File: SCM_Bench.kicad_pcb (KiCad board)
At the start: 4 copper layers, 294 parts, among them J1 Conn_Coaxial, J10 RF_Shield_One_Piece, J101 Conn_02x20_Odd_Even, J102 Conn_02x07_Odd_Even, J103 Conn_02x07_Odd_Even, J11 RF_Shield_One_Piece, J12 RF_Shield_One_Piece, J13 Conn_Coaxial, J14 Conn_Coaxial, J15 Conn_Coaxial, J16 Conn_Coaxial, J2 Conn_Coaxial, J3 Conn_Coaxial, J4 Conn_Coaxial, J5 Conn_Coaxial, J6 Conn_Coaxial, J7 RF_Shield_One_Piece, J8 RF_Shield_One_Piece, J9 RF_Shield_One_Piece, SW101 SW_Push, U1 LT6600IS8, U10 LT6600IS8, U101 ASDMB-xxxMHz, U11 LTC2386-18, U12 SN65LVDS1050PW, U13 LT6600IS8, U14 LTC2386-18, U15 SN65LVDS1050PW, U16 AD9747BCPZ, U17 SN65LVDS1DBV, U18 AD8021, U19 AD8021, U2 LTC2386-18, U20 AD9747BCPZ, U21 SN65LVDS1DBV, U22 AD8021, U23 AD8021, U3 SN65LVDS1050PW, U301 LT6600IS8, U302 LTC2386-18, U303 SN65LVDS1050PW, U4 LT6600IS8, U5 LTC2386-18, U6 SN65LVDS1050PW, U7 LT6600IS8, U8 LTC2386-18, U9 SN65LVDS1050PW

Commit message: initial placement of all ADC/DAC blocks and added FPGA
Signed-off-by: Alexis Jeandet <alexis.jeandet@member.fsf.org>
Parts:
- added C114: 100nF, Capacitor_SMD:C_0402_1005Metric, F.Cu at (56.0, 152.0)
- added C115: 100nF, Capacitor_SMD:C_0402_1005Metric, F.Cu at (53.1, 148.0)
- added C116: 100nF, Capacitor_SMD:C_0402_1005Metric, F.Cu at (53.1, 150.0)
- added C117: 100nF, Capacitor_SMD:C_0402_1005Metric, F.Cu at (56.0, 148.0)
- added C118: 100nF, Capacitor_SMD:C_0402_1005Metric, F.Cu at (60.4, 145.5)
- added C119: 100nF, Capacitor_SMD:C_0402_1005Metric, F.Cu at (53.1, 152.0)
- added C120: 100nF, Capacitor_SMD:C_0402_1005Metric, F.Cu at (56.0, 150.0)
- added C121: 100nF, Capacitor_SMD:C_0402_1005Metric, F.Cu at (58.9, 147.5)
- added C122: 100nF, Capacitor_SMD:C_0402_1005Metric, F.Cu at (53.1, 154.0)
- added C123: 100nF, Capacitor_SMD:C_0402_1005Metric, F.Cu at (63.3, 145.5)
- added C124: 100nF, Capacitor_SMD:C_0402_1005Metric, F.Cu at (58.9, 149.5)
- added C125: 100nF, Capacitor_SMD:C_0402_1005Metric, F.Cu at (57.4, 145.5)
- added C126: 100nF, Capacitor_SMD:C_0402_1005Metric, F.Cu at (61.8, 147.5)
- added C127: 100nF, Capacitor_SMD:C_0402_1005Metric, F.Cu at (53.1, 156.0)
- added C128: 100nF, Capacitor_SMD:C_0402_1005Metric, F.Cu at (56.0, 154.0)
- added C129: 100nF, Capacitor_SMD:C_0402_1005Metric, F.Cu at (58.9, 151.5)
- added C130: 100nF, Capacitor_SMD:C_0402_1005Metric, F.Cu at (66.2, 145.5)
- added C131: 100nF, Capacitor_SMD:C_0402_1005Metric, F.Cu at (53.1, 158.0)
- added DONE1: LED, Resistor_SMD:R_0603_1608Metric_Pad1.05x0.95mm_HandSolder, F.Cu at (53.8, 145.8)
- added R100: 10k, Resistor_SMD:R_0402_1005Metric, F.Cu at (61.8, 149.5)
- added R104: 10k, Resistor_SMD:R_0402_1005Metric, F.Cu at (64.7, 147.5)
- added R105: 2K2, Resistor_SMD:R_0402_1005Metric, F.Cu at (56.0, 156.0)
- added U24: ICE40HX1K-4K-TQ144, Package_QFP:TQFP-144_20x20mm_P0.5mm, F.Cu at (86.0, 152.0)
- C1, C10, C12, C13, C14, C15, C18, C19, C2, C20, C23, C25, C26, C301, C302, C305, C306, C307, C310, C312, C313, C5, C6, C7, J1, J2, J3, J7, J8, J9, R1, R11, R12, R14, R15, R16, R17, R18, R19, R2, R21, R24, R25, R3, R301, R302, R303, R304, R305, R306, R309, R311, R312, R4, R5, R6, R8, U1, U3, U301, U303, U4, U6: moved to B.Cu
- C11, C16, C17, C21, C22, C24, C3, C303, C304, C308, C309, C311, C4, C8, C9, R10, R13, R20, R22, R23, R26, R307, R308, R310, R313, R7, R9, U2, U302, U5: moved to F.Cu
- moved J16 345.7 mm to (141.2, 159.6), turned to 270 degrees
- moved J15 344.1 mm to (141.1, 169.1), turned to 270 degrees
- moved C107 332.1 mm to (131.2, 158.5), turned to 0 degrees
- moved R93 331.6 mm to (131.3, 161.1), turned to 180 degrees
- moved U22 331.5 mm to (131.3, 161.7), turned to 0 degrees
- moved C108 330.8 mm to (131.0, 163.6), turned to 0 degrees
- moved U23 330.6 mm to (131.3, 166.9), turned to 0 degrees
- moved C112 330.5 mm to (131.0, 165.0), turned to 0 degrees
- moved R99 330.5 mm to (131.3, 167.5), turned to 180 degrees
- moved C111 330.0 mm to (131.2, 170.2), turned to 0 degrees
- moved C109 327.6 mm to (128.1, 158.5), turned to 180 degrees
- moved C113 325.5 mm to (128.1, 170.2), turned to 180 degrees
- moved R90 324.2 mm to (126.0, 161.0), turned to 180 degrees
- moved R91 323.9 mm to (126.0, 162.5), turned to 180 degrees
- moved R92 323.9 mm to (126.0, 162.5), turned to 0 degrees
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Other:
- board outline added: 86 x 145 mm

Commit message: Layout done for ADC + LVDS and DAC -> FPGA
Signed-off-by: Alexis Jeandet <alexis.jeandet@member.fsf.org>
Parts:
- added C132: 100nF, Capacitor_SMD:C_0402_1005Metric, F.Cu at (103.9, 164.4)
- added J17: Conn_01x06, Connector_PinHeader_2.54mm:PinHeader_1x06_P2.54mm_Vertical, F.Cu at (80.2, 183.7)
- added R106: 10k, Resistor_SMD:R_0402_1005Metric, F.Cu at (105.3, 166.8)
- added R107: 10k, Resistor_SMD:R_0402_1005Metric, B.Cu at (96.3, 168.5)
- added R108: 10k, Resistor_SMD:R_0402_1005Metric, B.Cu at (96.6, 166.0)
- added U25: M25PX32-VMW, Package_SO:SOIJ-8_5.3x5.3mm_P1.27mm, F.Cu at (99.8, 167.9)
- C114, C116, C117, C118, C119, C120, C121, C124, C125, C126, C127, C129, C130, C131, R100, R104, R105, R38: moved to B.Cu
- R312: moved to F.Cu
- moved C101 69.6 mm to (55.6, 71.2)
- moved C102 69.6 mm to (43.7, 78.2)
- moved D101 69.6 mm to (53.4, 69.0)
- moved D102 69.6 mm to (44.4, 75.9)
- moved H101 69.6 mm to (47.7, 71.2)
- moved H102 69.6 mm to (38.8, 76.3)
- moved R101 69.6 mm to (46.6, 79.6)
- moved R102 69.6 mm to (57.0, 68.7)
- moved R103 69.6 mm to (52.7, 71.2)
- moved SW101 69.6 mm to (39.8, 70.3)
- moved U101 69.6 mm to (48.6, 76.7)
- moved R39 51.0 mm to (64.1, 67.2), turned to 90 degrees
- moved C38 48.5 mm to (66.9, 70.0), turned to 180 degrees
- moved U9 46.3 mm to (69.0, 66.3), turned to 180 degrees
- moved C115 45.5 mm to (96.2, 162.8)
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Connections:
- J1 pad 1: /Sheet5F3E1819/CH1_IN+ -> /Sheet5F3E1819/CH2_IN+
- J1 pad 2: /Sheet5F3E1819/CH1_IN- -> /Sheet5F3E1819/CH2_IN-
- J2 pad 1: /Sheet5F3E1819/CH2_IN+ -> /Sheet5F3E1819/CH6_IN+
- J2 pad 2: /Sheet5F3E1819/CH2_IN- -> /Sheet5F3E1819/CH6_IN-
- J3 pad 1: /Sheet5F3E1819/CH3_IN+ -> /Sheet5F3E1819/CH4_IN+
- J3 pad 2: /Sheet5F3E1819/CH3_IN- -> /Sheet5F3E1819/CH4_IN-
- J4 pad 1: /Sheet5F3E1819/CH4_IN+ -> /Sheet5F3E1819/CH1_IN+
- J4 pad 2: /Sheet5F3E1819/CH4_IN- -> /Sheet5F3E1819/CH1_IN-
- J6 pad 1: /Sheet5F3E1819/CH6_IN+ -> /Sheet5F3E1819/CH3_IN+
- J6 pad 2: /Sheet5F3E1819/CH6_IN- -> /Sheet5F3E1819/CH3_IN-
- R1 pad 2: /Sheet5F3E1819/CH2_IN+ -> /Sheet5F3E1819/CH6_IN+
- R104 pad 1: /Sheet5F420A25/sheet5F62EEDA/FLASH_SS -> VCCIO_0
- R104 pad 2: GND -> /Sheet5F420A25/sheet5F62EEDA/FLASH_CLK
- R14 pad 2: /Sheet5F3E1819/CH3_IN+ -> /Sheet5F3E1819/CH4_IN+
- R15 pad 2: /Sheet5F3E1819/CH3_IN- -> /Sheet5F3E1819/CH4_IN-
- R2 pad 2: /Sheet5F3E1819/CH2_IN- -> /Sheet5F3E1819/CH6_IN-
- R27 pad 2: /Sheet5F3E1819/CH4_IN+ -> /Sheet5F3E1819/CH1_IN+
- R28 pad 2: /Sheet5F3E1819/CH4_IN- -> /Sheet5F3E1819/CH1_IN-
- R301 pad 2: /Sheet5F3E1819/CH1_IN+ -> /Sheet5F3E1819/CH2_IN+
- R302 pad 2: /Sheet5F3E1819/CH1_IN- -> /Sheet5F3E1819/CH2_IN-
- R53 pad 2: /Sheet5F3E1819/CH6_IN+ -> /Sheet5F3E1819/CH3_IN+
- R54 pad 2: /Sheet5F3E1819/CH6_IN- -> /Sheet5F3E1819/CH3_IN-
- U16 pad 10: (no net) -> /Sheet5F420A25/DAC1_D14
- U16 pad 11: (no net) -> /Sheet5F420A25/DAC1_D13
- U16 pad 12: (no net) -> /Sheet5F420A25/DAC1_D12
- U16 pad 13: (no net) -> /Sheet5F420A25/DAC1_D11
- U16 pad 14: (no net) -> /Sheet5F420A25/DAC1_D10
- U16 pad 15: (no net) -> /Sheet5F420A25/DAC1_D9
- U16 pad 16: (no net) -> /Sheet5F420A25/DAC1_D8
- U16 pad 17: (no net) -> /Sheet5F420A25/DAC1_D7
- U16 pad 18: (no net) -> /Sheet5F420A25/DAC1_D6
- U16 pad 19: (no net) -> /Sheet5F420A25/DAC1_D5
- U16 pad 20: (no net) -> /Sheet5F420A25/DAC1_D4
- U16 pad 21: (no net) -> /Sheet5F420A25/DAC1_D3
- U16 pad 22: (no net) -> /Sheet5F420A25/DAC1_D2
- U16 pad 23: (no net) -> /Sheet5F420A25/DAC1_D1
- U16 pad 24: (no net) -> /Sheet5F420A25/DAC1_D0
- U16 pad 25: (no net) -> /Sheet5F420A25/sheet5F62EEDA/DAC1_DCO
- U16 pad 29: (no net) -> /Sheet5F420A25/sheet5F62EEDA/DAC1_IQSEL
- U16 pad 49: (no net) -> /Sheet5F420A25/sheet5F62EEDA/DAC1_SDO
- U16 pad 50: (no net) -> /Sheet5F420A25/sheet5F62EEDA/DAC1_SDIO
- U16 pad 51: (no net) -> /Sheet5F420A25/sheet5F62EEDA/DAC1_SCLK
- U16 pad 52: (no net) -> /Sheet5F420A25/Sheet5F420DB3/CSB
- U16 pad 53: (no net) -> /Sheet5F420A25/sheet5F62EEDA/DAC1_RST
- U16 pad 9: (no net) -> /Sheet5F420A25/DAC1_D15
- U17 pad 5: (no net) -> /Sheet5F420A25/sheet5F62EEDA/DAC1_CLK
- U20 pad 10: (no net) -> /Sheet5F420A25/DAC2_D14
- U20 pad 11: (no net) -> /Sheet5F420A25/DAC2_D13
- U20 pad 12: (no net) -> /Sheet5F420A25/DAC2_D12
- U20 pad 13: (no net) -> /Sheet5F420A25/DAC2_D11
- U20 pad 14: (no net) -> /Sheet5F420A25/DAC2_D10
- U20 pad 15: (no net) -> /Sheet5F420A25/DAC2_D9
- U20 pad 16: (no net) -> /Sheet5F420A25/DAC2_D8
- U20 pad 17: (no net) -> /Sheet5F420A25/DAC2_D7
- U20 pad 18: (no net) -> /Sheet5F420A25/DAC2_D6
- U20 pad 19: (no net) -> /Sheet5F420A25/DAC2_D5
- U20 pad 20: (no net) -> /Sheet5F420A25/DAC2_D4
- U20 pad 21: (no net) -> /Sheet5F420A25/DAC2_D3
- U20 pad 22: (no net) -> /Sheet5F420A25/DAC2_D2
- U20 pad 23: (no net) -> /Sheet5F420A25/DAC2_D1
- U20 pad 24: (no net) -> /Sheet5F420A25/DAC2_D0
- U20 pad 25: (no net) -> /Sheet5F420A25/sheet5F62EEDA/DAC2_DCO
- U20 pad 29: (no net) -> /Sheet5F420A25/sheet5F62EEDA/DAC2_IQSEL
- U20 pad 49: (no net) -> /Sheet5F420A25/sheet5F62EEDA/DAC2_SDO
- U20 pad 50: (no net) -> /Sheet5F420A25/sheet5F62EEDA/DAC2_SDIO
- U20 pad 51: (no net) -> /Sheet5F420A25/sheet5F62EEDA/DAC2_SCLK
- U20 pad 52: (no net) -> /Sheet5F420A25/sheet5F604603/CSB
- U20 pad 53: (no net) -> /Sheet5F420A25/sheet5F62EEDA/DAC2_RST
- U20 pad 9: (no net) -> /Sheet5F420A25/DAC2_D15
- U21 pad 5: (no net) -> /Sheet5F420A25/sheet5F62EEDA/DAC2_CLK
- U24 pad 101: (no net) -> /Sheet5F420A25/sheet5F62EEDA/DAC2_CLK
- U24 pad 102: (no net) -> /Sheet5F420A25/sheet5F62EEDA/DAC1_RST
- U24 pad 104: (no net) -> /Sheet5F420A25/Sheet5F420DB3/CSB
- U24 pad 105: (no net) -> /Sheet5F420A25/sheet5F62EEDA/DAC1_SCLK
- U24 pad 106: (no net) -> /Sheet5F420A25/sheet5F62EEDA/DAC1_SDIO
- U24 pad 107: (no net) -> /Sheet5F420A25/sheet5F62EEDA/DAC1_SDO
- U24 pad 112: (no net) -> /Sheet5F420A25/sheet5F62EEDA/DAC1_IQSEL
- U24 pad 113: (no net) -> /Sheet5F420A25/DAC1_D0
- U24 pad 114: (no net) -> /Sheet5F420A25/DAC1_D1
- U24 pad 115: (no net) -> /Sheet5F420A25/DAC1_D2
- U24 pad 116: (no net) -> /Sheet5F420A25/DAC1_D3
- U24 pad 117: (no net) -> /Sheet5F420A25/DAC1_D4
- U24 pad 118: (no net) -> /Sheet5F420A25/DAC1_D5
- U24 pad 119: (no net) -> /Sheet5F420A25/DAC1_D6
- U24 pad 120: (no net) -> /Sheet5F420A25/DAC1_D7
- U24 pad 121: (no net) -> /Sheet5F420A25/DAC1_D8
- U24 pad 122: (no net) -> /Sheet5F420A25/DAC1_D9
- U24 pad 128: (no net) -> /Sheet5F420A25/sheet5F62EEDA/DAC1_DCO
- U24 pad 129: (no net) -> /Sheet5F420A25/DAC1_D10
- U24 pad 134: (no net) -> /Sheet5F420A25/DAC1_D11
- U24 pad 135: (no net) -> /Sheet5F420A25/DAC1_D12
- U24 pad 136: (no net) -> /Sheet5F420A25/DAC1_D13
- U24 pad 137: (no net) -> /Sheet5F420A25/DAC1_D14
- U24 pad 138: (no net) -> /Sheet5F420A25/DAC1_D15
- U24 pad 139: (no net) -> /Sheet5F420A25/sheet5F62EEDA/DAC1_CLK
- U24 pad 58: (no net) -> /Sheet5F420A25/sheet5F604603/CSB
- U24 pad 60: (no net) -> /Sheet5F420A25/sheet5F62EEDA/DAC2_SCLK
- U24 pad 61: (no net) -> /Sheet5F420A25/sheet5F62EEDA/DAC2_SDIO
- U24 pad 62: (no net) -> /Sheet5F420A25/sheet5F62EEDA/DAC2_SDO
- U24 pad 67: (no net) -> /Sheet5F420A25/sheet5F62EEDA/FLASH_MISO
- U24 pad 68: (no net) -> /Sheet5F420A25/sheet5F62EEDA/FLASH_MOSI
- U24 pad 70: (no net) -> /Sheet5F420A25/sheet5F62EEDA/FLASH_CLK
- U24 pad 73: (no net) -> /Sheet5F420A25/sheet5F62EEDA/DAC2_RST
- U24 pad 74: (no net) -> /Sheet5F420A25/sheet5F62EEDA/DAC2_IQSEL
- U24 pad 75: (no net) -> /Sheet5F420A25/DAC2_D0
- U24 pad 76: (no net) -> /Sheet5F420A25/DAC2_D1
- U24 pad 78: (no net) -> /Sheet5F420A25/DAC2_D2
- U24 pad 79: (no net) -> /Sheet5F420A25/DAC2_D3
- U24 pad 80: (no net) -> /Sheet5F420A25/DAC2_D4
- U24 pad 81: (no net) -> /Sheet5F420A25/DAC2_D5
- U24 pad 87: (no net) -> /Sheet5F420A25/DAC2_D6
- U24 pad 88: (no net) -> /Sheet5F420A25/DAC2_D7
- U24 pad 90: (no net) -> /Sheet5F420A25/DAC2_D8
- U24 pad 91: (no net) -> /Sheet5F420A25/DAC2_D9
- U24 pad 93: (no net) -> /Sheet5F420A25/sheet5F62EEDA/DAC2_DCO
- U24 pad 94: (no net) -> /Sheet5F420A25/DAC2_D10
- U24 pad 95: (no net) -> /Sheet5F420A25/DAC2_D11
- U24 pad 96: (no net) -> /Sheet5F420A25/DAC2_D12
- U24 pad 97: (no net) -> /Sheet5F420A25/DAC2_D13
- U24 pad 98: (no net) -> /Sheet5F420A25/DAC2_D14
- U24 pad 99: (no net) -> /Sheet5F420A25/DAC2_D15
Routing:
- net /Sheet5F3E1819/sheet5F7672A2/CNV+: track 0.00 -> 92.7 mm, vias 0 -> 1
- net /Sheet5F3E1819/sheet5F7672A2/CNV-: track 0.00 -> 89.5 mm, vias 0 -> 1
- net /Sheet5F3E1819/sheet5F7672A2/CLK+: track 2.41 -> 75.3 mm, vias 0 -> 1
- net /Sheet5F3E1819/sheet5F7672A2/CLK-: track 2.78 -> 75.1 mm, vias 0 -> 1
- net /Sheet5F3E1819/sheet5F7672A2/DCO+: track 0.00 -> 65.4 mm, vias 0 -> 1
- net /Sheet5F3E1819/sheet5F7672A2/DA+: track 0.00 -> 65.0 mm, vias 0 -> 1
- net /Sheet5F3E1819/sheet5F7672A2/DA-: track 0.00 -> 64.7 mm, vias 0 -> 1
- net /Sheet5F3E1819/sheet5F7672A2/DCO-: track 0.00 -> 63.0 mm, vias 0 -> 1
- net /Sheet5F3E1819/Sheet5F3E1AE4/DA-: track 0.00 -> 49.7 mm, vias 0 -> 1
- net /Sheet5F3E1819/Sheet5F3E1AE4/DA+: track 0.00 -> 48.1 mm, vias 0 -> 1
- net /Sheet5F420A25/sheet5F62EEDA/DAC1_CLK: track 0.00 -> 47.6 mm, vias 0 -> 2
- net /Sheet5F420A25/DAC1_D15: track 0.00 -> 46.2 mm
- net /Sheet5F420A25/DAC1_D14: track 0.00 -> 44.4 mm
- net /Sheet5F420A25/DAC1_D13: track 0.00 -> 42.7 mm
- net /Sheet5F420A25/DAC1_D12: track 0.00 -> 41.0 mm
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
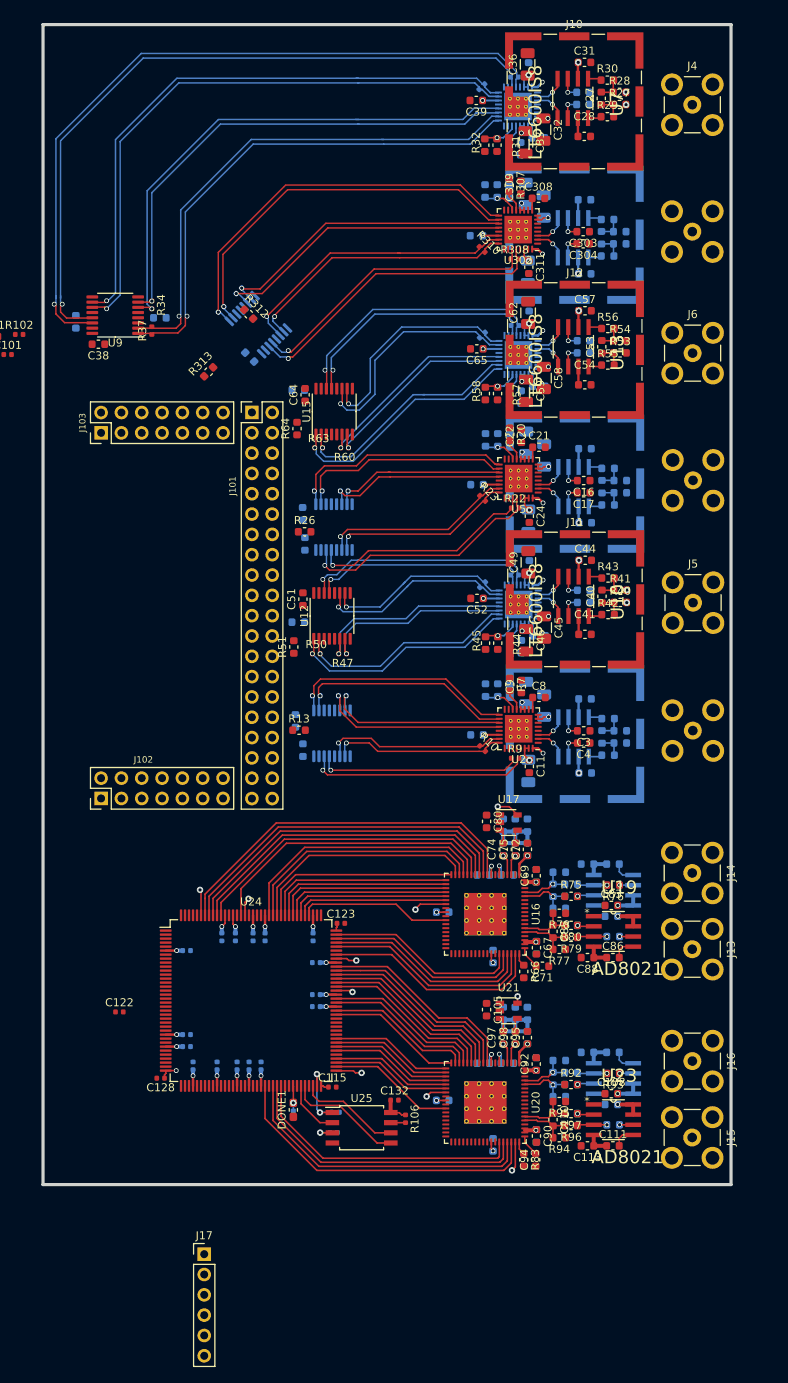
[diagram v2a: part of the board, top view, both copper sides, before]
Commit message: Added #3.3V and #1.2V supply, completed ADC to USB board layout, added DAC FPGA to USB board bus.
Signed-off-by: Alexis Jeandet <alexis.jeandet@member.fsf.org>
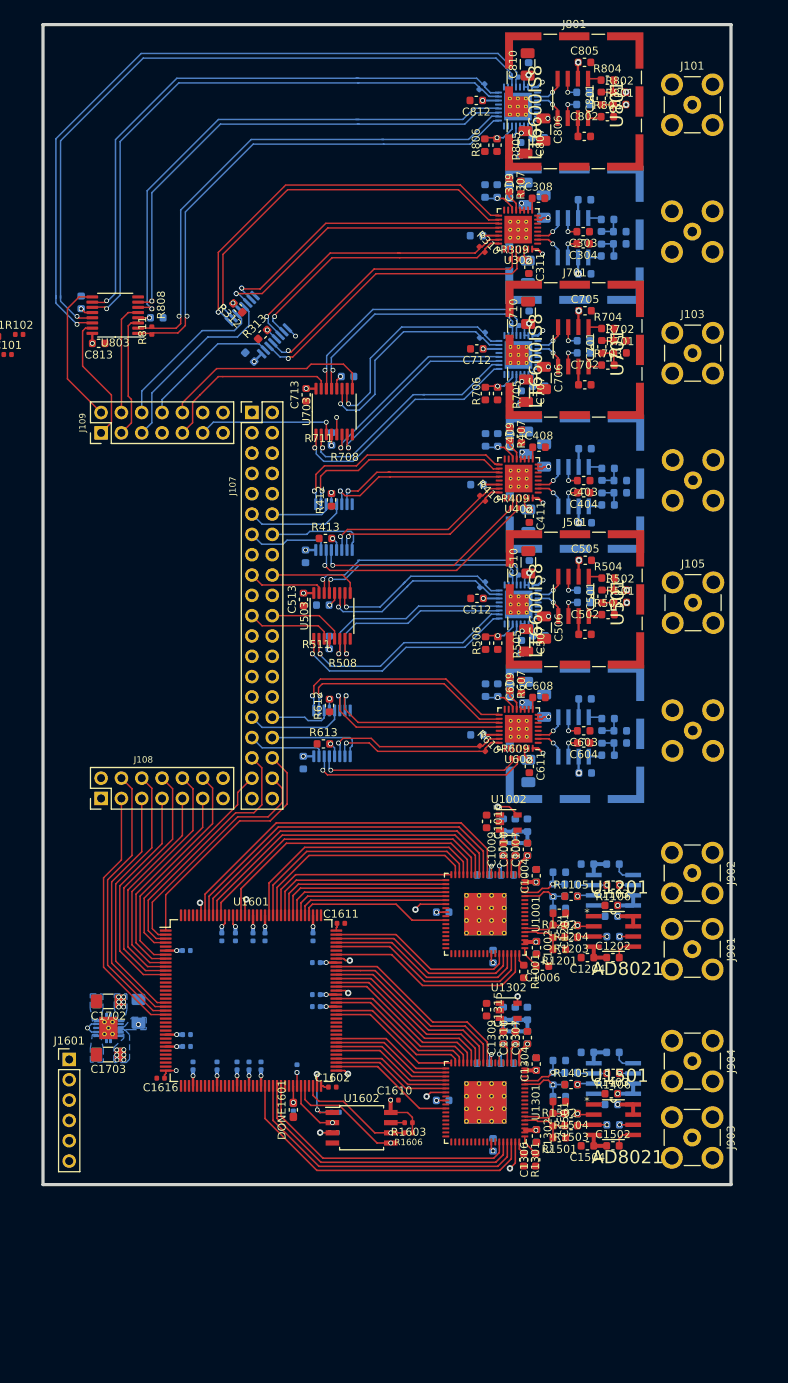
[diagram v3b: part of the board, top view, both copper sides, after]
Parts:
- removed C122: 100nF, Capacitor_SMD:C_0402_1005Metric
- removed R38: 10k, Resistor_SMD:R_0603_1608Metric
- added C1609: 100nF, Capacitor_SMD:C_0402_1005Metric, B.Cu at (77.9, 145.7)
- added C1620: 100nF, Capacitor_SMD:C_0402_1005Metric, B.Cu at (78.0, 157.7)
- added C1701: 10uF, Capacitor_SMD:C_1206_3216Metric_Pad1.42x1.75mm_HandSolder, B.Cu at (71.9, 153.3)
- added C1702: 10uF, Capacitor_SMD:C_1206_3216Metric_Pad1.42x1.75mm_HandSolder, F.Cu at (68.2, 152.1)
- added C1703: 10uF, Capacitor_SMD:C_1206_3216Metric_Pad1.42x1.75mm_HandSolder, F.Cu at (68.2, 158.8)
- added L1701: 2.2uH, Inductor_SMD:L_1206_3216Metric_Pad1.42x1.75mm_HandSolder, B.Cu at (68.2, 158.8)
- added L1702: 2.2uH, Inductor_SMD:L_1206_3216Metric_Pad1.42x1.75mm_HandSolder, B.Cu at (68.2, 152.1)
- added R812: 10k, Resistor_SMD:R_0603_1608Metric, B.Cu at (74.2, 66.6)
- added U1701: tps6240x, Package_SON:Texas_S-PVSON-N10_ThermalVias, B.Cu at (68.2, 155.4)
- R1606: renamed from R104; moved to F.Cu
- R412: renamed from R25; moved to F.Cu
- R512: renamed from R51; moved to B.Cu
- R612: renamed from R12; moved to F.Cu
- R712: renamed from R64; moved to B.Cu
- moved R1606 35.9 mm to (105.7, 168.5), turned to 180 degrees
- moved J1601 29.6 mm to (63.3, 159.4)
- moved R1601 14.1 mm to (91.7, 160.5), turned to 270 degrees
- moved R313 8.21 mm to (87.5, 68.7)
- moved R713 6.40 mm to (98.1, 74.0), turned to 180 degrees
- moved R612 4.67 mm to (95.8, 115.1), turned to 90 degrees
- moved R712 4.50 mm to (96.1, 81.8), turned to 270 degrees
- moved R512 4.47 mm to (95.8, 107.2), turned to 270 degrees
- moved R412 4.01 mm to (96.1, 89.4), turned to 90 degrees
- moved R513 3.74 mm to (95.0, 102.6)
- moved R613 3.50 mm to (95.0, 119.9)
- moved R413 2.73 mm to (95.3, 94.2)
- moved R813 2.52 mm to (64.8, 64.7), turned to 270 degrees
- moved R312 1.56 mm to (84.4, 65.4), turned to 135 degrees
- moved C413 1.56 mm to (92.8, 96.5), turned to 90 degrees
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- renumbered C66 to C1001, C67 to C1002, C68 to C1003, C69 to C1004, C70 to C1005, C71 to C1006, C72 to C1007, C73 to C1008, C74 to C1009, C75 to C1010, C76 to C1011, C77 to C1012, C78 to C1013, C79 to C1014, C80 to C1015, C81 to C1101, C82 to C1102, C83 to C1103, C84 to C1104, C85 to C1201, C86 to C1202, C87 to C1203, C88 to C1204, C89 to C1301, C90 to C1302, C91 to C1303, C92 to C1304, C93 to C1305, C94 to C1306, C95 to C1307, C96 to C1308, C97 to C1309, C98 to C1310, C99 to C1311, C100 to C1312, C103 to C1313, C104 to C1314, C105 to C1315, C106 to C1401, C107 to C1402, C108 to C1403, C109 to C1404, C110 to C1501, C111 to C1502, C112 to C1503, C113 to C1504, C114 to C1601, C115 to C1602, C116 to C1603, C117 to C1604, C118 to C1605, C119 to C1606, C120 to C1607, C121 to C1608, C132 to C1610, C123 to C1611, C124 to C1612, C125 to C1613, C126 to C1614, C127 to C1615, C128 to C1616, C129 to C1617, C130 to C1618, C131 to C1619, C307 to C305, C305 to C306, C306 to C307, C14 to C401, C15 to C402, C16 to C403, C17 to C404, C18 to C405, C19 to C406, C20 to C407, C21 to C408, C22 to C409, C23 to C410, C24 to C411, C26 to C412, C25 to C413, C40 to C501, C41 to C502, C42 to C503, C43 to C504, C44 to C505, C45 to C506, C46 to C507, C47 to C508, C48 to C509, C49 to C510, C50 to C511, C52 to C512, C51 to C513, C1 to C601, C2 to C602, C3 to C603, C4 to C604, C5 to C605, C6 to C606, C7 to C607, C8 to C608, C9 to C609, C10 to C610, C11 to C611, C13 to C612, C12 to C613, C53 to C701, C54 to C702, C55 to C703, C56 to C704, C57 to C705, C58 to C706, C59 to C707, C60 to C708, C61 to C709, C62 to C710, C63 to C711, C65 to C712, C64 to C713, C27 to C801, C28 to C802, C29 to C803, C30 to C804, C31 to C805, C32 to C806, C33 to C807, C34 to C808, C35 to C809, C36 to C810, C37 to C811, C39 to C812, C38 to C813, DONE1 to DONE1601, J4 to J101, J1 to J102, J6 to J103, J3 to J104, J5 to J105, J2 to J106, J101 to J107, J102 to J108, J103 to J109, J17 to J1601, J7 to J301, J9 to J401, J11 to J501, J8 to J601, J12 to J701, J10 to J801, J13 to J901, J14 to J902, J15 to J903, J16 to J904, R66 to R1001, R67 to R1002, R68 to R1003, R69 to R1004, R70 to R1005, R71 to R1101, R72 to R1102, R73 to R1103, R74 to R1104, R75 to R1105, R76 to R1106, R77 to R1201, R78 to R1202, R79 to R1203, R80 to R1204, R81 to R1205, R82 to R1206, R83 to R1301, R84 to R1302, R85 to R1303, R86 to R1304, R87 to R1305, R88 to R1401, R89 to R1402, R90 to R1403, R91 to R1404, R92 to R1405, R93 to R1406, R94 to R1501, R95 to R1502, R96 to R1503, R97 to R1504, R98 to R1505, R99 to R1506, R100 to R1601, R105 to R1602, R106 to R1603, R107 to R1604, R108 to R1605, R309 to R308, R308 to R309, R14 to R401, R15 to R402, R16 to R403, R17 to R404, R18 to R405, R19 to R406, R20 to R407, R21 to R408, R22 to R409, R23 to R410, R24 to R411, R26 to R413, R40 to R501, R41 to R502, R42 to R503, R43 to R504, R44 to R505, R45 to R506, R46 to R507, R47 to R508, R48 to R509, R49 to R510, R50 to R511, R52 to R513, R1 to R601, R2 to R602, R3 to R603, R4 to R604, R5 to R605, R6 to R606, R7 to R607, R8 to R608, R9 to R609, R10 to R610, R11 to R611, R13 to R613, R53 to R701, R54 to R702, R55 to R703, R56 to R704, R57 to R705, R58 to R706, R59 to R707, R60 to R708, R61 to R709, R62 to R710, R63 to R711, R65 to R713, R27 to R801, R28 to R802, R29 to R803, R30 to R804, R31 to R805, R32 to R806, R33 to R807, R34 to R808, R35 to R809, R36 to R810, R37 to R811, R39 to R813, U16 to U1001, U17 to U1002, U18 to U1101, U19 to U1201, U20 to U1301, U21 to U1302, U22 to U1401, U23 to U1501, U24 to U1601, U25 to U1602, U4 to U401, U5 to U402, U6 to U403, U10 to U501, U11 to U502, U12 to U503, U1 to U601, U2 to U602, U3 to U603, U13 to U701, U14 to U702, U15 to U703, U7 to U801, U8 to U802, U9 to U803
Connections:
- net /Sheet5F420A25/sheet5F62EEDA/2.5V renamed /Sheet5F420A25/#2.5V
- C1005 pad 1: /Sheet5F420A25/Sheet5F420DB3/DVDD33 -> VCCIO_0
- C1305 pad 1: /Sheet5F420A25/sheet5F604603/DVDD33 -> VCCIO_0
- J107 pad 11: (no net) -> /ADC4_DCO
- J107 pad 12: (no net) -> /ADC4_DA
- J107 pad 13: (no net) -> /ADC4_CNV
- J107 pad 14: (no net) -> /ADC4_CLK
- J107 pad 17: (no net) -> /ADC5_CNV
- J107 pad 18: (no net) -> /ADC5_CLK
- J107 pad 21: (no net) -> /ADC5_DA
- J107 pad 22: (no net) -> /ADC5_DCO
- J107 pad 26: (no net) -> /FLASH_~CRESET
- J107 pad 27: (no net) -> /FLASH_SS
- J107 pad 28: (no net) -> /FLASH_CLK
- J107 pad 29: (no net) -> /FLASH_MISO
- J107 pad 30: (no net) -> /FLASH_MOSI
- J107 pad 31: (no net) -> /ADC6_DCO
- J107 pad 32: (no net) -> /ADC6_DA
- J107 pad 33: (no net) -> /ADC6_CNV
- J107 pad 34: (no net) -> /ADC6_CLK
- J107 pad 35: (no net) -> /DAC_FPGA_IO2
- J107 pad 36: (no net) -> /DAC_FPGA_IO0
- J107 pad 37: (no net) -> /DAC_FPGA_IO3
- J107 pad 38: (no net) -> /DAC_FPGA_IO1
- J108 pad 10: (no net) -> /DAC_FPGA_IO6
- J108 pad 11: (no net) -> /DAC_FPGA_IO5
- J108 pad 12: (no net) -> /DAC_FPGA_IO4
- J108 pad 3: (no net) -> /DAC_FPGA_IO13
- J108 pad 4: (no net) -> /DAC_FPGA_IO12
- J108 pad 5: (no net) -> /DAC_FPGA_IO11
- J108 pad 6: (no net) -> /DAC_FPGA_IO10
- J108 pad 7: (no net) -> /DAC_FPGA_IO9
- J108 pad 8: (no net) -> /DAC_FPGA_IO8
- J108 pad 9: (no net) -> /DAC_FPGA_IO7
- J109 pad 1: (no net) -> /ADC1_CNV
- J109 pad 10: (no net) -> /ADC3_CLK
- J109 pad 11: (no net) -> /ADC3_DA
- J109 pad 12: (no net) -> /ADC3_DCO
- J109 pad 2: (no net) -> /ADC1_CLK
- J109 pad 3: (no net) -> /ADC1_DA
- J109 pad 4: (no net) -> /ADC1_DCO
- J109 pad 5: (no net) -> /ADC2_DCO
- J109 pad 6: (no net) -> /ADC2_DA
- J109 pad 7: (no net) -> /ADC2_CLK
- J109 pad 8: (no net) -> /ADC2_CNV
- J109 pad 9: (no net) -> /ADC3_CNV
- J1601 pad 1: /Sheet5F420A25/sheet5F62EEDA/FLASH_~CRESET -> /FLASH_~CRESET
- J1601 pad 2: /Sheet5F420A25/sheet5F62EEDA/FLASH_SS -> /FLASH_SS
- J1601 pad 3: /Sheet5F420A25/sheet5F62EEDA/FLASH_CLK -> /FLASH_CLK
- J1601 pad 4: /Sheet5F420A25/sheet5F62EEDA/FLASH_MISO -> /FLASH_MISO
- J1601 pad 5: /Sheet5F420A25/sheet5F62EEDA/FLASH_MOSI -> /FLASH_MOSI
- R1601 pad 2: /Sheet5F420A25/sheet5F62EEDA/FLASH_~CRESET -> /FLASH_~CRESET
- R1605 pad 2: /Sheet5F420A25/sheet5F62EEDA/FLASH_SS -> /FLASH_SS
- R1606 pad 2: /Sheet5F420A25/sheet5F62EEDA/FLASH_CLK -> /FLASH_CLK
- U1001 pad 27: /Sheet5F420A25/Sheet5F420DB3/DVDD33 -> VCCIO_0
- U1301 pad 27: /Sheet5F420A25/sheet5F604603/DVDD33 -> VCCIO_0
- U1601 pad 1: (no net) -> /DAC_FPGA_IO0
- U1601 pad 10: (no net) -> /DAC_FPGA_IO7
- U1601 pad 11: (no net) -> /DAC_FPGA_IO8
- U1601 pad 12: (no net) -> /DAC_FPGA_IO9
- U1601 pad 19: (no net) -> /DAC_FPGA_IO10
- U1601 pad 2: (no net) -> /DAC_FPGA_IO1
- U1601 pad 20: (no net) -> /DAC_FPGA_IO11
- U1601 pad 21: (no net) -> /DAC_FPGA_IO12
- U1601 pad 22: (no net) -> /DAC_FPGA_IO13
- U1601 pad 3: (no net) -> /DAC_FPGA_IO2
- U1601 pad 4: (no net) -> /DAC_FPGA_IO3
- U1601 pad 66: /Sheet5F420A25/sheet5F62EEDA/FLASH_~CRESET -> /FLASH_~CRESET
- U1601 pad 67: /Sheet5F420A25/sheet5F62EEDA/FLASH_MISO -> /FLASH_MISO
- U1601 pad 68: /Sheet5F420A25/sheet5F62EEDA/FLASH_MOSI -> /FLASH_MOSI
- U1601 pad 7: (no net) -> /DAC_FPGA_IO4
- U1601 pad 70: /Sheet5F420A25/sheet5F62EEDA/FLASH_CLK -> /FLASH_CLK
- U1601 pad 71: /Sheet5F420A25/sheet5F62EEDA/FLASH_SS -> /FLASH_SS
- U1601 pad 8: (no net) -> /DAC_FPGA_IO5
- U1601 pad 9: (no net) -> /DAC_FPGA_IO6
- U1602 pad 1: /Sheet5F420A25/sheet5F62EEDA/FLASH_SS -> /FLASH_SS
- U1602 pad 2: /Sheet5F420A25/sheet5F62EEDA/FLASH_MISO -> /FLASH_MISO
- U1602 pad 5: /Sheet5F420A25/sheet5F62EEDA/FLASH_MOSI -> /FLASH_MOSI
- U1602 pad 6: /Sheet5F420A25/sheet5F62EEDA/FLASH_CLK -> /FLASH_CLK
- U303 pad 15: (no net) -> /ADC2_CNV
- U303 pad 3: (no net) -> /ADC2_DA
- U303 pad 5: (no net) -> /ADC2_DCO
- U303 pad 9: (no net) -> /ADC2_CLK
- U403 pad 15: (no net) -> /ADC4_CNV
- U403 pad 3: (no net) -> /ADC4_DA
- U403 pad 5: (no net) -> /ADC4_DCO
- U403 pad 9: (no net) -> /ADC4_CLK
- U503 pad 15: (no net) -> /ADC5_CNV
- U503 pad 3: (no net) -> /ADC5_DA
- U503 pad 5: (no net) -> /ADC5_DCO
- U503 pad 9: (no net) -> /ADC5_CLK
- U603 pad 15: (no net) -> /ADC6_CNV
- U603 pad 3: (no net) -> /ADC6_DA
- U603 pad 5: (no net) -> /ADC6_DCO
- U603 pad 9: (no net) -> /ADC6_CLK
- U703 pad 15: (no net) -> /ADC3_CNV
- U703 pad 3: (no net) -> /ADC3_DA
- U703 pad 5: (no net) -> /ADC3_DCO
- U703 pad 9: (no net) -> /ADC3_CLK
- U803 pad 15: (no net) -> /ADC1_CNV
- U803 pad 3: (no net) -> /ADC1_DA
- U803 pad 5: (no net) -> /ADC1_DCO
- U803 pad 9: (no net) -> /ADC1_CLK
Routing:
- net /FLASH_MOSI: track 0.00 -> 133.7 mm, vias 0 -> 1
- net /FLASH_CLK: track 0.00 -> 132.9 mm, vias 0 -> 1
- net /FLASH_MISO: track 0.00 -> 115.2 mm, vias 0 -> 1
- net /FLASH_SS: track 0.00 -> 114.5 mm, vias 0 -> 2
- net /FLASH_~CRESET: track 0.00 -> 106.6 mm, vias 0 -> 1
- net /DAC_FPGA_IO12: track 0.00 -> 34.8 mm
- net /DAC_FPGA_IO10: track 0.00 -> 33.7 mm
- net /DAC_FPGA_IO13: track 0.00 -> 32.2 mm
- net /DAC_FPGA_IO2: track 0.00 -> 31.9 mm
- net /DAC_FPGA_IO11: track 0.00 -> 31.2 mm
- net /DAC_FPGA_IO0: track 0.00 -> 30.9 mm
- net /DAC_FPGA_IO8: track 0.00 -> 30.8 mm
- net /DAC_FPGA_IO1: track 0.00 -> 30.3 mm
- net /DAC_FPGA_IO6: track 0.00 -> 29.7 mm
- net /DAC_FPGA_IO4: track 0.00 -> 28.5 mm
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- added copper zone on B.Cu, net /USB_5V
- added copper zone on B.Cu, net Net-(L1701-Pad1)
- added copper zone on B.Cu, net Net-(L1702-Pad1)
- added copper zone on B.Cu, net VCC
- added copper zone on B.Cu, net VCCIO_0
